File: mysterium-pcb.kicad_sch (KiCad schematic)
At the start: 219 parts, among them J1 AVR-ISP-6, J2 Conn_01x04, SW0 KEYSW, SW1 KEYSW, SW10 KEYSW, SW100 KEYSW, SW101 KEYSW, SW102 KEYSW, SW103 Rotary_Encoder_Switch, SW11 KEYSW, SW12 KEYSW, SW13 KEYSW, SW14 KEYSW, SW15 KEYSW, SW16 KEYSW, SW17 KEYSW, SW18 KEYSW, SW19 KEYSW, SW2 KEYSW, SW20 KEYSW, SW21 KEYSW, SW22 KEYSW, SW23 KEYSW, SW24 KEYSW, SW25 KEYSW, SW26 KEYSW, SW27 KEYSW, SW28 KEYSW, SW29 KEYSW, SW3 KEYSW, SW30 KEYSW, SW31 KEYSW, SW32 KEYSW, SW33 KEYSW, SW34 KEYSW, SW35 KEYSW, SW36 KEYSW, SW37 KEYSW, SW38 KEYSW, SW39 KEYSW, SW4 KEYSW, SW40 KEYSW, SW41 KEYSW, SW42 KEYSW, SW43 KEYSW, SW44 KEYSW, SW45 KEYSW, SW46 KEYSW, SW47 KEYSW, SW48 KEYSW, SW49 KEYSW, SW5 KEYSW, SW50 KEYSW, SW51 KEYSW, SW52 KEYSW, SW53 KEYSW, SW54 KEYSW, SW55 KEYSW, SW56 KEYSW, SW57 KEYSW, SW58 KEYSW, SW59 KEYSW, SW6 KEYSW, SW60 KEYSW, SW61 KEYSW, SW62 KEYSW, SW63 KEYSW, SW64 KEYSW, SW65 KEYSW, SW66 KEYSW, SW67 KEYSW, SW68 KEYSW, SW69 KEYSW, SW7 KEYSW, SW70 KEYSW, SW71 KEYSW, SW72 KEYSW, SW73 KEYSW, SW74 KEYSW, SW75 KEYSW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

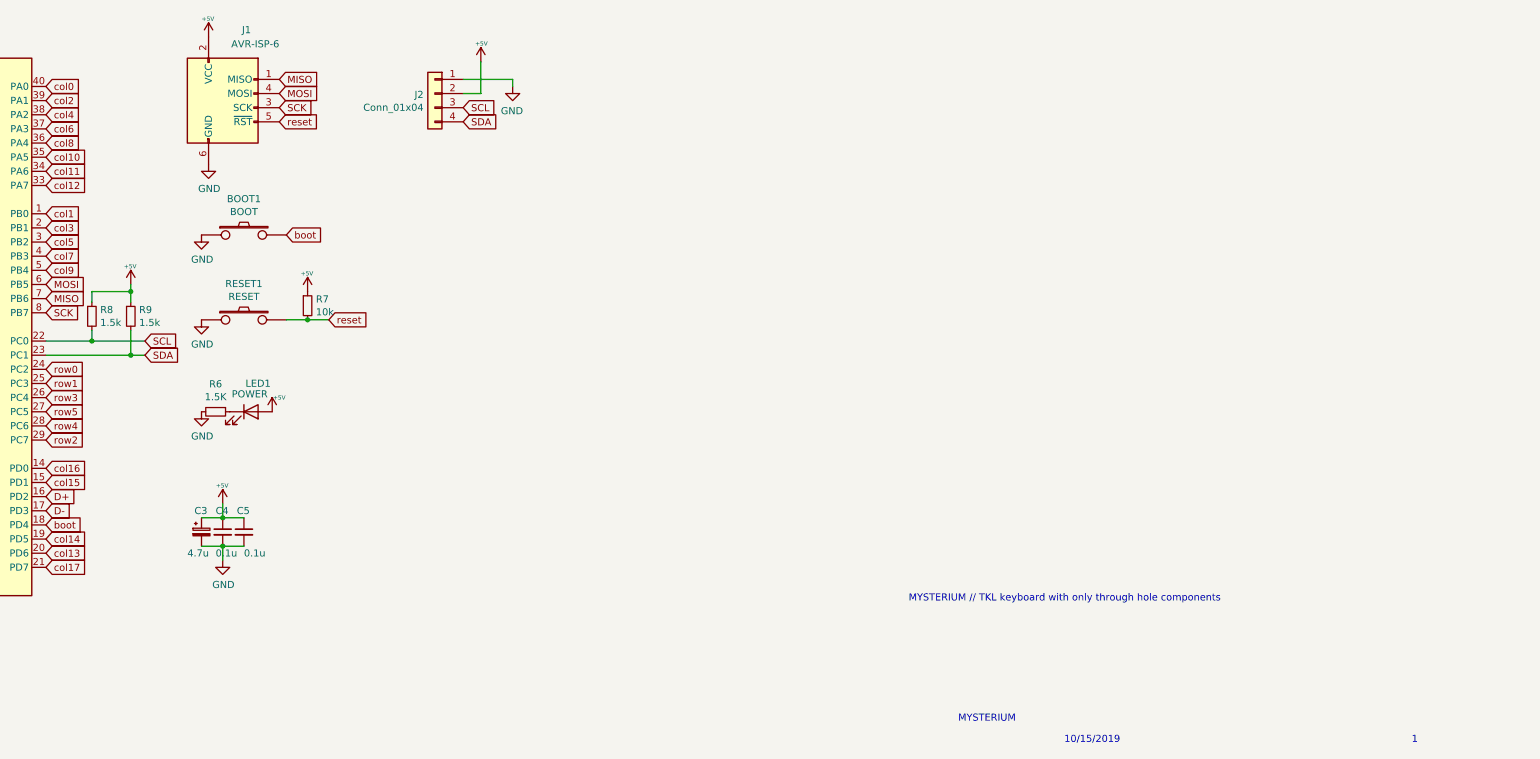
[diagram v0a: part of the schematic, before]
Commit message: PCB: add second TRRS socket on the left; use 5.1k I2C pullups
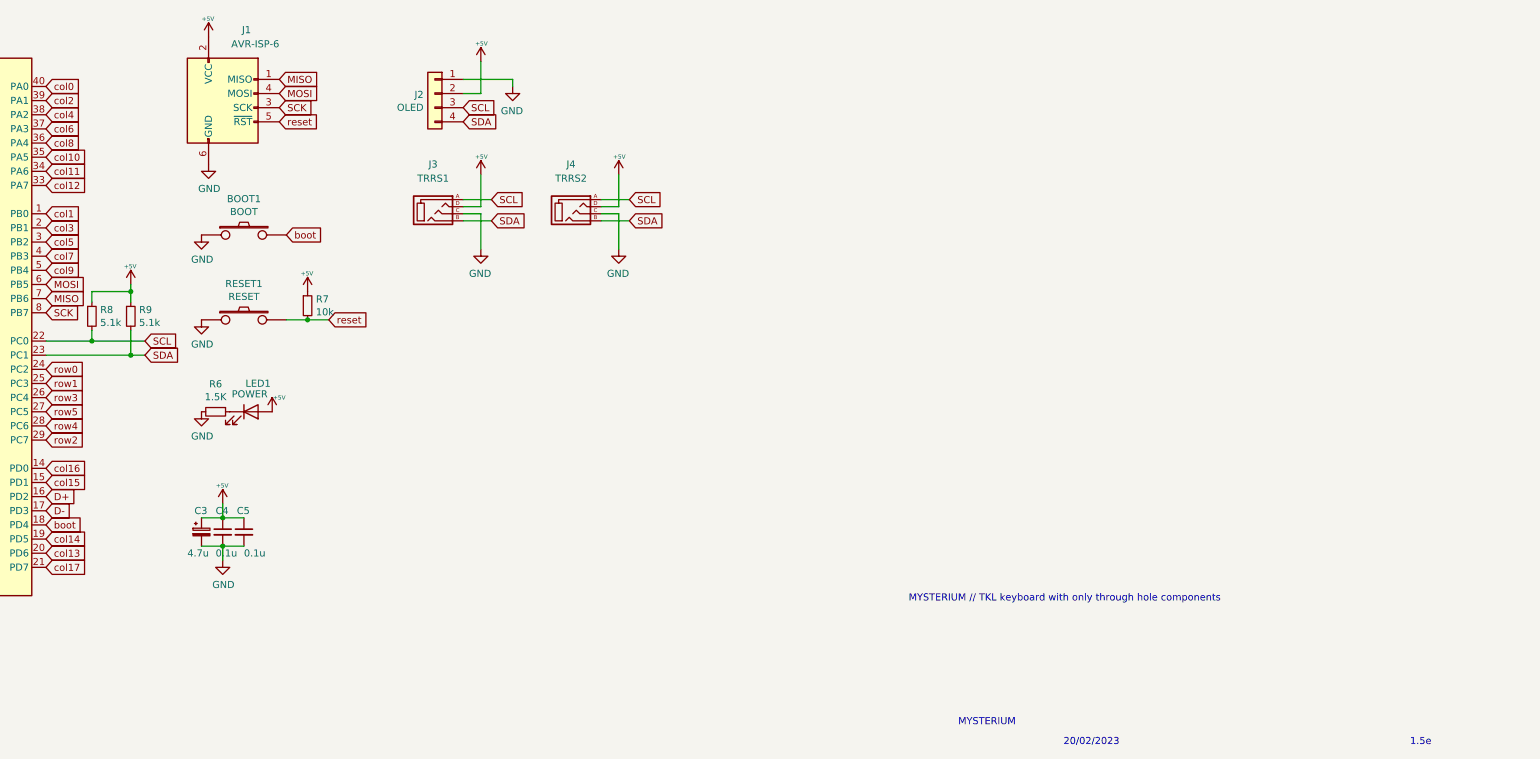
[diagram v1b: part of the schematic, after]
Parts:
- added J3: TRRS1, kbd:MJ-4PP-9_1side, symbol kbd:MJ-4PP-9
- added J4: TRRS2, kbd:MJ-4PP-9_1side, symbol kbd:MJ-4PP-9
- J2: value Conn_01x04 -> OLED
- R8, R9: value 1.5k -> 5.1k
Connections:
- net +5V: now also J3.D, J4.D
- net GND: now also J3.C, J4.C
- net SCL: now also J3.A, J4.A
- net SDA: now also J3.B, J4.B
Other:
- note added: "1.5e"
- note added: "20/02/2023"
- note removed: "1"
- note removed: "10/15/2019"

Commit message: Fix diode footprints, resolve DRC errors/warnings
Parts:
- D95, D96: footprint cftkb:D_DO-35_SOD27_P5.08mm_Horizontal -> cftkb:D_DO-35_SOD27_P5.08mm_Horizontal_Zener
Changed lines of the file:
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@@
       (effects (font (size 0.9906 0.9906)) (justify left))
     )
-    (property "Footprint" "cftkb:D_DO-35_SOD27_P5.08mm_Horizontal" (id 2) (at 74.93 184.15 90)
+    (property "Footprint" "cftkb:D_DO-35_SOD27_P5.08mm_Horizontal_Zener" (id 2) (at 74.93 184.15 90)
       (effects (font (size 1.27 1.27)) hide)
     )
@@
       (effects (font (size 0.9906 0.9906)) (justify left))
     )
-    (property "Footprint" "cftkb:D_DO-35_SOD27_P5.08mm_Horizontal" (id 2) (at 77.47 184.15 90)
+    (property "Footprint" "cftkb:D_DO-35_SOD27_P5.08mm_Horizontal_Zener" (id 2) (at 77.47 184.15 90)
       (effects (font (size 1.27 1.27)) hide)
     )
@@
     )
     (path "/00000000-0000-0000-0000-00005d184b7b"
-      (reference "D95") (unit 1) (value "3.6V") (footprint "cftkb:D_DO-35_SOD27_P5.08mm_Horizontal")
+      (reference "D95") (unit 1) (value "3.6V") (footprint "cftkb:D_DO-35_SOD27_P5.08mm_Horizontal_Zener")
     )
     (path "/00000000-0000-0000-0000-00005d184d75"
-      (reference "D96") (unit 1) (value "3.6V") (footprint "cftkb:D_DO-35_SOD27_P5.08mm_Horizontal")
+      (reference "D96") (unit 1) (value "3.6V") (footprint "cftkb:D_DO-35_SOD27_P5.08mm_Horizontal_Zener")
     )
     (path "/00000000-0000-0000-0000-000060dcf1d3"
